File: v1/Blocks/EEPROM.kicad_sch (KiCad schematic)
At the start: 1 part, among them U2 AT24CM02-SSHM-B

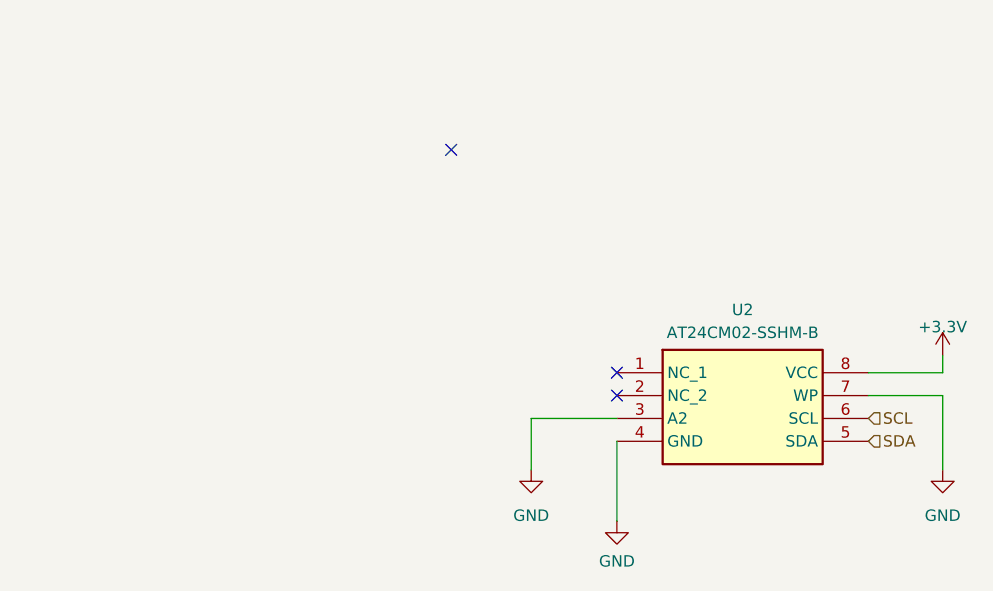
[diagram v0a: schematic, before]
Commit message: Update views, to make drawing sheets smaller where necessary
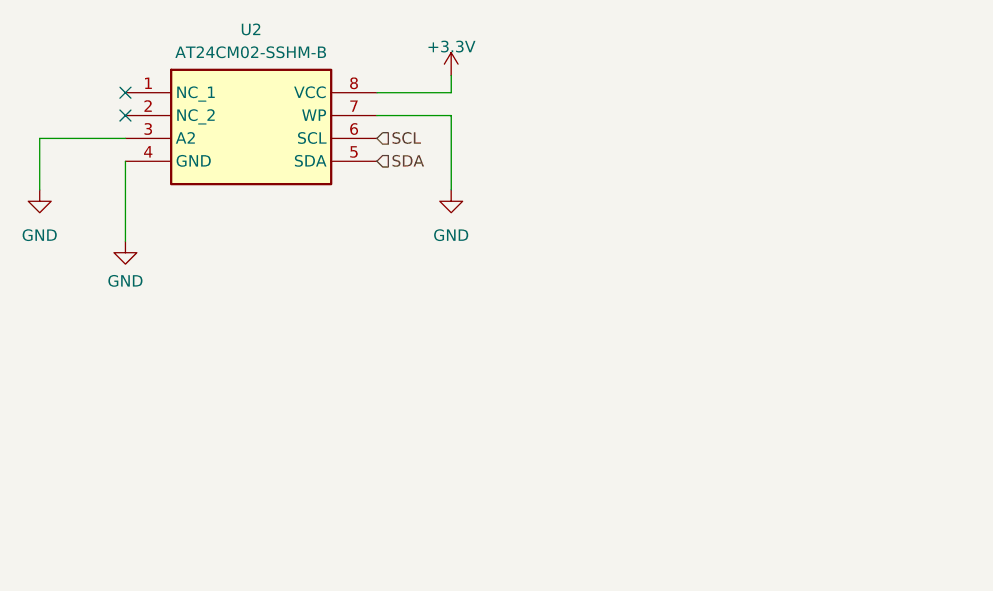
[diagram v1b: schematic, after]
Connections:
- no-connect marks 3 -> 2
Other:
- moved on the sheet: U2
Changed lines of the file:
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@@
 (kicad_sch (version 20230121) (generator eeschema)
-  (paper "A4")
-  (no_connect (at 140.97 100.965))
-  (no_connect (at 122.555 73.66))
-  (no_connect (at 140.97 98.425))
-  (wire (pts (xy 168.91 100.965) (xy 177.165 100.965))
+  (paper "A5")
+  (no_connect (at 86.36 69.85))
+  (no_connect (at 86.36 67.31))
+  (wire (pts (xy 114.3 69.85) (xy 122.555 69.85))
     (stroke (width 0) (type default))
   )
-  (wire (pts (xy 177.165 100.965) (xy 177.165 109.22))
+  (wire (pts (xy 122.555 69.85) (xy 122.555 78.105))
     (stroke (width 0) (type default))
   )
-  (wire (pts (xy 140.97 103.505) (xy 131.445 103.505))
+  (wire (pts (xy 86.36 72.39) (xy 76.835 72.39))
     (stroke (width 0) (type default))
   )
-  (wire (pts (xy 177.165 98.425) (xy 168.91 98.425))
+  (wire (pts (xy 122.555 67.31) (xy 114.3 67.31))
     (stroke (width 0) (type default))
   )
-  (wire (pts (xy 177.165 96.52) (xy 177.165 98.425))
+  (wire (pts (xy 122.555 65.405) (xy 122.555 67.31))
     (stroke (width 0) (type default))
   )
-  (wire (pts (xy 140.97 106.045) (xy 140.97 114.935))
+  (wire (pts (xy 86.36 74.93) (xy 86.36 83.82))
     (stroke (width 0) (type default))
   )
-  (wire (pts (xy 131.445 103.505) (xy 131.445 109.22))
+  (wire (pts (xy 76.835 72.39) (xy 76.835 78.105))
     (stroke (width 0) (type default))
   )
-  (hierarchical_label "SCL" (shape input) (at 168.91 103.505 0) (fields_autoplaced)
+  (hierarchical_label "SCL" (shape input) (at 114.3 72.39 0) (fields_autoplaced)
     (effects (font (size 1.27 1.27)) (justify left))
   )
-  (hierarchical_label "SDA" (shape input) (at 168.91 106.045 0) (fields_autoplaced)
+  (hierarchical_label "SDA" (shape input) (at 114.3 74.93 0) (fields_autoplaced)
     (effects (font (size 1.27 1.27)) (justify left))
   )
-  (symbol (lib_id "power:GND") (at 177.165 109.22 0) (unit 1)
+  (symbol (lib_id "power:GND") (at 122.555 78.105 0) (unit 1)
     (in_bom yes) (on_board yes) (dnp no) (fields_autoplaced)
-    (property "Reference" "#PWR0133" (at 177.165 115.57 0)
+    (property "Reference" "#PWR0133" (at 122.555 84.455 0)
       (effects (font (size 1.27 1.27)) hide)
     )
-    (property "Value" "GND" (at 177.165 114.3 0)
+    (property "Value" "GND" (at 122.555 83.185 0)
       (effects (font (size 1.27 1.27)))
     )
-    (property "Footprint" "" (at 177.165 109.22 0)
+    (property "Footprint" "" (at 122.555 78.105 0)
       (effects (font (size 1.27 1.27)) hide)
     )
-    (property "Datasheet" "" (at 177.165 109.22 0)
+    (property "Datasheet" "" (at 122.555 78.105 0)
       (effects (font (size 1.27 1.27)) hide)
     )
@@
     )
   )
-  (symbol (lib_id "power:+3.3V") (at 177.165 96.52 0) (unit 1)
+  (symbol (lib_id "power:+3.3V") (at 122.555 65.405 0) (unit 1)
     (in_bom yes) (on_board yes) (dnp no) (fields_autoplaced)
-    (property "Reference" "#PWR0134" (at 177.165 100.33 0)
+    (property "Reference" "#PWR0134" (at 122.555 69.215 0)
       (effects (font (size 1.27 1.27)) hide)
     )
-    (property "Value" "+3.3V" (at 177.165 93.345 0)
+    (property "Value" "+3.3V" (at 122.555 62.23 0)
       (effects (font (size 1.27 1.27)))
     )
-    (property "Footprint" "" (at 177.165 96.52 0)
+    (property "Footprint" "" (at 122.555 65.405 0)
       (effects (font (size 1.27 1.27)) hide)
     )
-    (property "Datasheet" "" (at 177.165 96.52 0)
+    (property "Datasheet" "" (at 122.555 65.405 0)
       (effects (font (size 1.27 1.27)) hide)
     )
@@
     )
   )
-  (symbol (lib_id "AT24CM02-SSHM-B:AT24CM02-SSHM-B") (at 140.97 98.425 0) (unit 1)
+  (symbol (lib_id "AT24CM02-SSHM-B:AT24CM02-SSHM-B") (at 86.36 67.31 0) (unit 1)
     (in_bom yes) (on_board yes) (dnp no) (fields_autoplaced)
-    (property "Reference" "U2" (at 154.94 91.44 0)
+    (property "Reference" "U2" (at 100.33 60.325 0)
       (effects (font (size 1.27 1.27)))
     )
-    (property "Value" "AT24CM02-SSHM-B" (at 154.94 93.98 0)
+    (property "Value" "AT24CM02-SSHM-B" (at 100.33 62.865 0)
       (effects (font (size 1.27 1.27)))
     )
-    (property "Footprint" "AT24CM02-SSHM-B:SOIC127P600X175-8N" (at 165.1 193.345 0)
+    (property "Footprint" "AT24CM02-SSHM-B:SOIC127P600X175-8N" (at 110.49 162.23 0)
       (effects (font (size 1.27 1.27)) (justify left top) hide)
     )
-    (property "Datasheet" "https://www.mouser.co.id/datasheet/2/268/Atmel-8828-SEEPROM-AT24CM02-Datasheet-1398087.pdf" (at 165.1 293.345 0)
+    (property "Datasheet" "https://www.mouser.co.id/datasheet/2/268/Atmel-8828-SEEPROM-AT24CM02-Datasheet-1398087.pdf" (at 110.49 262.23 0)
       (effects (font (size 1.27 1.27)) (justify left top) hide)
     )
-    (property "Height" "1.75" (at 165.1 493.345 0)
+    (property "Height" "1.75" (at 110.49 462.23 0)
       (effects (font (size 1.27 1.27)) (justify left top) hide)
     )
-    (property "Mouser Part Number" "579-AT24CM02-SSHM-B" (at 165.1 593.345 0)
+    (property "Mouser Part Number" "579-AT24CM02-SSHM-B" (at 110.49 562.23 0)
       (effects (font (size 1.27 1.27)) (justify left top) hide)
     )
-    (property "Mouser Price/Stock" "https://www.mouser.co.uk/ProductDetail/Microchip-Technology-Atmel/AT24CM02-SSHM-B?qs=PUo64BuKcKhyyKfULTKDLw%3D%3D" (at 165.1 693.345 0)
+    (property "Mouser Price/Stock" "https://www.mouser.co.uk/ProductDetail/Microchip-Technology-Atmel/AT24CM02-SSHM-B?qs=PUo64BuKcKhyyKfULTKDLw%3D%3D" (at 110.49 662.23 0)
       (effects (font (size 1.27 1.27)) (justify left top) hide)
     )
-    (property "Manufacturer_Name" "Microchip" (at 165.1 793.345 0)
+    (property "Manufacturer_Name" "Microchip" (at 110.49 762.23 0)
       (effects (font (size 1.27 1.27)) (justify left top) hide)
     )
-    (property "Manufacturer_Part_Number" "AT24CM02-SSHM-B" (at 165.1 893.345 0)
+    (property "Manufacturer_Part_Number" "AT24CM02-SSHM-B" (at 110.49 862.23 0)
       (effects (font (size 1.27 1.27)) (justify left top) hide)
     )
@@
     )
   )
-  (symbol (lib_id "power:GND") (at 140.97 114.935 0) (unit 1)
+  (symbol (lib_id "power:GND") (at 86.36 83.82 0) (unit 1)
     (in_bom yes) (on_board yes) (dnp no) (fields_autoplaced)
-    (property "Reference" "#PWR0135" (at 140.97 121.285 0)
+    (property "Reference" "#PWR0135" (at 86.36 90.17 0)
       (effects (font (size 1.27 1.27)) hide)
     )
-    (property "Value" "GND" (at 140.97 119.38 0)
+    (property "Value" "GND" (at 86.36 88.265 0)
       (effects (font (size 1.27 1.27)))
     )
-    (property "Footprint" "" (at 140.97 114.935 0)
+    (property "Footprint" "" (at 86.36 83.82 0)
       (effects (font (size 1.27 1.27)) hide)
     )
-    (property "Datasheet" "" (at 140.97 114.935 0)
+    (property "Datasheet" "" (at 86.36 83.82 0)
       (effects (font (size 1.27 1.27)) hide)
     )
@@
     )
   )
-  (symbol (lib_id "power:GND") (at 131.445 109.22 0) (unit 1)
+  (symbol (lib_id "power:GND") (at 76.835 78.105 0) (unit 1)
     (in_bom yes) (on_board yes) (dnp no) (fields_autoplaced)
-    (property "Reference" "#PWR0132" (at 131.445 115.57 0)
+    (property "Reference" "#PWR0132" (at 76.835 84.455 0)
       (effects (font (size 1.27 1.27)) hide)
     )
-    (property "Value" "GND" (at 131.445 114.3 0)
+    (property "Value" "GND" (at 76.835 83.185 0)
       (effects (font (size 1.27 1.27)))
     )
-    (property "Footprint" "" (at 131.445 109.22 0)
+    (property "Footprint" "" (at 76.835 78.105 0)
       (effects (font (size 1.27 1.27)) hide)
     )
-    (property "Datasheet" "" (at 131.445 109.22 0)
+    (property "Datasheet" "" (at 76.835 78.105 0)
       (effects (font (size 1.27 1.27)) hide)
     )
